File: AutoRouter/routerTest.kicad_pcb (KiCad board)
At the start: 2 copper layers, 104 x 83.9 mm, 30 parts

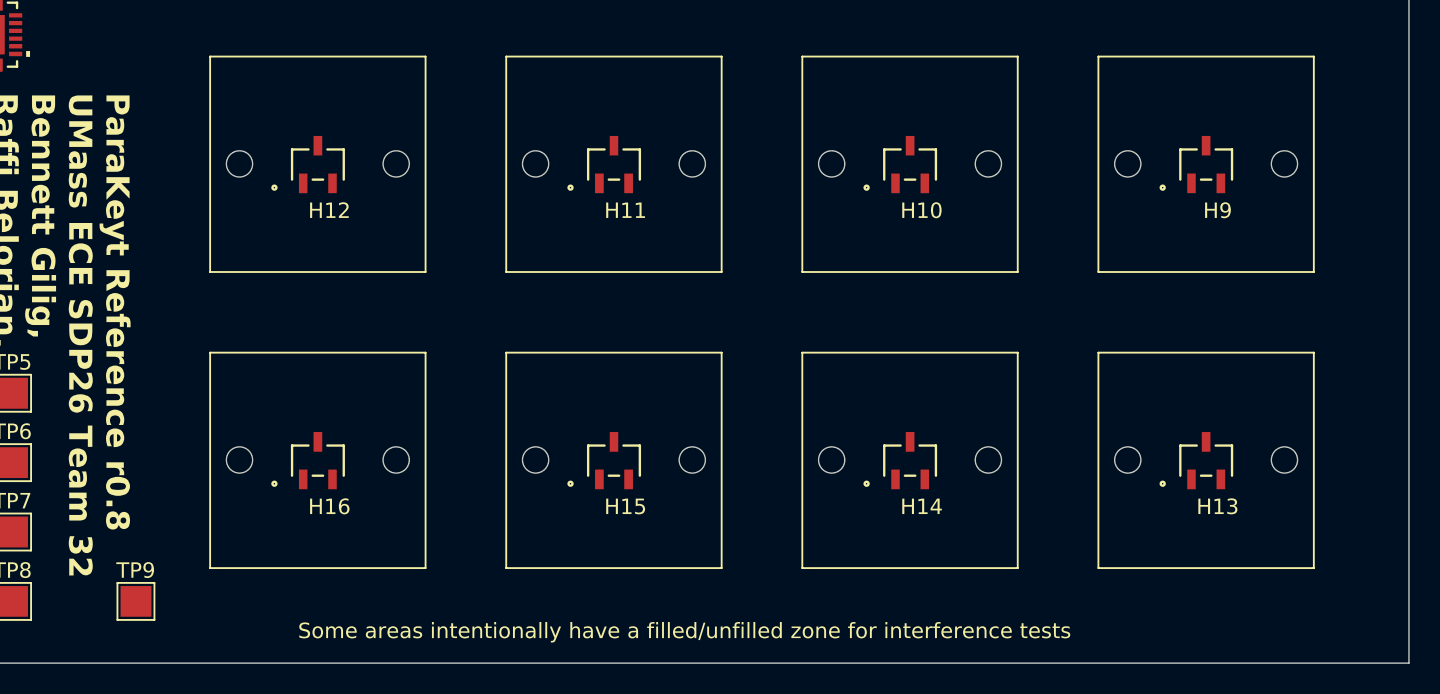
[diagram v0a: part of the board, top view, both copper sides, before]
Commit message: added ground plane logic to back of pcb
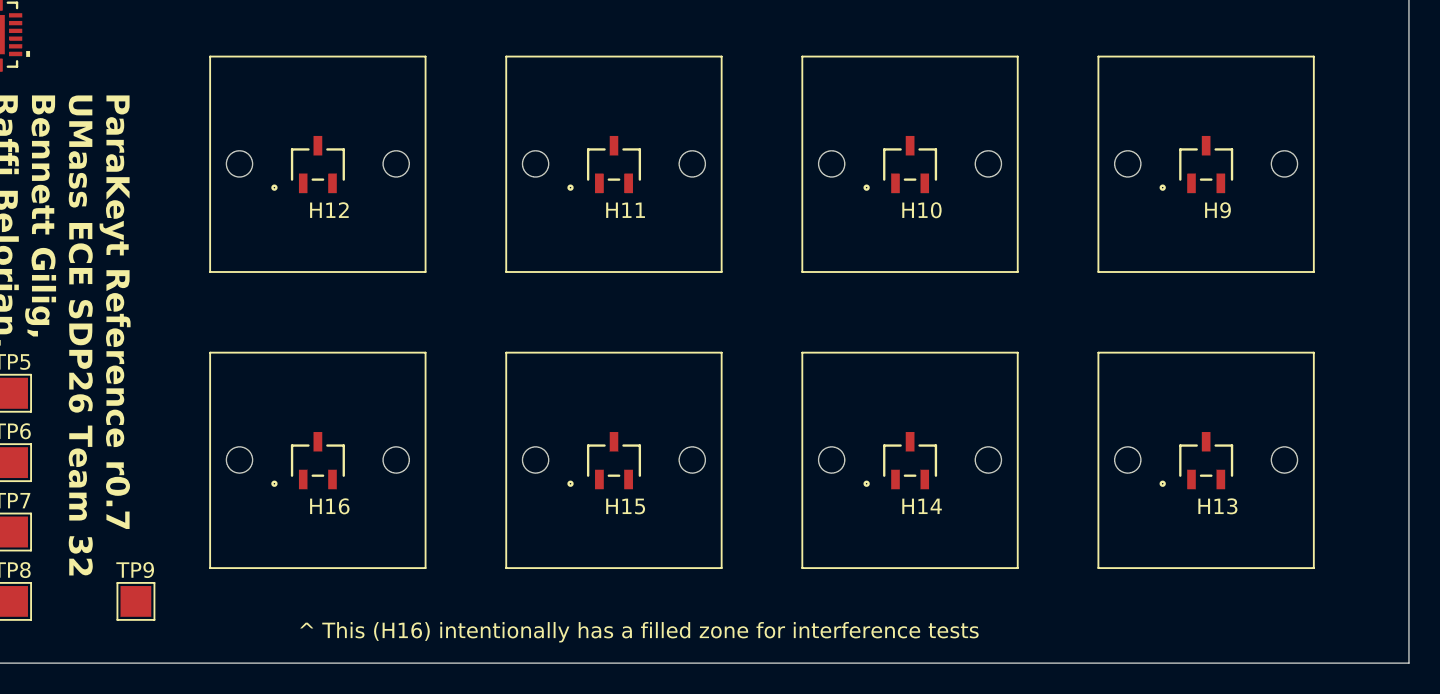
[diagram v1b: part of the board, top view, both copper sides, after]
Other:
- board text added: "ParaKeyt Reference r0.7 UMass ECE SDP26 Team 32 Bennett Gilig, Raffi Belorian, Rikhav Shah, Shlok Raval, Theo Krueger. THIS SIDE FACE DOWN"
- board text added: "^ This (H16) intentionally has a filled zone for interference tests"
- board text removed: "ParaKeyt Reference r0.8 UMass ECE SDP26 Team 32 Bennett Gilig, Raffi Belorian, Rikhav Shah, Shlok Raval, Theo Krueger. THIS SIDE FACE DOWN"
- board text removed: "Some areas intentionally have a filled/unfilled zone for interference tests"
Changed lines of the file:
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@@
 	(title_block
 		(title "ParaKeyt Reference Design")
-		(date "2025-11-05")
-		(rev "0.8")
+		(date "2025-10-30")
+		(rev "0.7")
 		(company "UMass ECE SDP26 Team 32")
 		(comment 1 "Bennett Gilig, Raffi Belorian, Rikhav Shah, Shlok Raval, Theo Krueger")
@@
 		)
 		(fp_rect
-			(start -10 -12.5)
-			(end 10 12.5)
+			(start -10.4 -12.75)
+			(end 10.9 13.25)
 			(stroke
-				(width 0.05)
+				(width 0.1)
 				(type default)
 			)
 			(fill no)
-			(layer "F.CrtYd")
+			(layer "Margin")
 		)
 		(pad "1" thru_hole oval
@@
 		(layer "Edge.Cuts")
 	)
-	(gr_text "Some areas intentionally have a filled/unfilled zone for interference tests"
+	(gr_text "^ This (H16) intentionally has a filled zone for interference tests"
 		(at 44 94.5 0)
 		(layer "F.SilkS")
@@
 		)
 	)
-	(gr_text "ParaKeyt Reference r0.8\nUMass ECE SDP26 Team 32\nBennett Gilig,\nRaffi Belorian,\nRikhav Shah,\nShlok Raval,\nTheo Krueger.\nTHIS SIDE FACE DOWN"
+	(gr_text "ParaKeyt Reference r0.7\nUMass ECE SDP26 Team 32\nBennett Gilig,\nRaffi Belorian,\nRikhav Shah,\nShlok Raval,\nTheo Krueger.\nTHIS SIDE FACE DOWN"
 		(at 14.5 59 270)
 		(layer "F.SilkS")
